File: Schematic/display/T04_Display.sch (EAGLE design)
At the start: 42 parts, among them IC1 4514D, Q1 2N7002, Q2 2N7002, Q3 2N7002, Q4 2N7002, Q5 2N7002, Q6 2N7002, Q7 2N7002, Q8 2N7002, Q9 2N7002

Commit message: V1.1 Schematic, with latches
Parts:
- removed IC1: 4514D, 45xx:4514D
- removed Q1, Q2, Q3, Q4, Q5, Q6, Q7, Q8, Q9: 2N7002, transistor-power:BUZ11BV
- removed R10, R12, R14, R16, R18: 150, resistor:R-US_M3516
- removed R11, R13, R15, R17: 4.7k, resistor:R-US_M3516
- added C10, C11, C12, C13, C14, C5, C6, C7, C8, C9: (no value), resistor:C-EUC1206
- added U$1, U$10, U$12, U$13, U$4, U$5, U$6, U$8, U$9: 2N7002, display:2N7002
- added U$11, U$2, U$7: CD4043, display:CD4043
- added U$3: HEF4067B, display:HEF4067B
- C1, C2, C3, C4: value 0.1u -> (none); device eagle-ltspice:CC3216 -> resistor:C-EUC1206
- LED1, LED4, LED7: value LTL1CHKGKNN -> (none); device led:LEDSMT1206 -> display:LED3MM
- LED2, LED5, LED8: value LTL1CHKSKNN -> (none); device led:LEDSMT1206 -> display:LED3MM
- LED3, LED6, LED9: value LTL1CHKEKNN -> (none); device led:LEDSMT1206 -> display:LED3MM
- R1, R3, R5, R7, R9: value 4.7k -> (none); device resistor:R-US_M3516 -> rcl:R-US_R1206
- R2, R4, R6, R8: value 150 -> (none); device resistor:R-US_M3516 -> rcl:R-US_R1206
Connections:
- removed net +5V: C1.1, C2.1, C3.1, C4.1, IC1A.ST, IC1P.VDD, Q1.D, Q2.D, Q3.D, Q4.D, Q5.D, Q6.D, Q7.D, Q8.D, Q9.D, SV1.2
- removed net BIT0: IC1A.D1, SV1.6
- removed net BIT1: IC1A.D2, SV1.5
- removed net BIT2: IC1A.D3, SV1.4
- removed net BIT3: IC1A.D4, SV1.3
- removed net N$20: LED6.A, R12.1
- removed net N$21: Q7.S, R14.2
- removed net N$24: Q8.S, R16.2
- removed net N$26: Q9.S, R18.2
- removed net N$27: LED9.A, R18.1
- removed net N$28: LED8.A, R16.1
- removed net N$29: LED7.A, R14.1
- removed net N$36: IC1A.S0, Q1.G, R1.2
- removed net N$37: IC1A.S1, Q2.G, R3.2
- removed net N$38: IC1A.S2, Q3.G, R5.2
- removed net N$39: IC1A.S3, Q4.G, R7.2
- removed net N$40: IC1A.S4, Q5.G, R9.2
- removed net N$41: IC1A.S5, Q6.G, R11.2
- removed net N$42: IC1A.S6, Q7.G, R13.2
- removed net N$43: IC1A.S7, Q8.G, R15.2
- removed net N$44: IC1A.S8, Q9.G, R17.2
- new net A0: SV1.6, U$3.A0
- new net A1: SV1.5, U$3.A1
- new net A2: SV1.4, U$3.A2
- new net A3: SV1.3, U$3.A3
- new net BG: U$10.G, U$11.Q1
- new net BR: U$11.Q3, U$13.G
- new net BRES: U$11.R1, U$11.R2, U$11.R3, U$11.R4, U$3.Y3
- new net BS1: U$11.S1, U$3.Y0
- new net BS2: U$11.S2, U$3.Y1
- new net BS3: U$11.S3, U$3.Y2
- new net BY: U$11.Q2, U$12.G
- new net LG: U$1.G, U$2.Q1
- new net LR: U$2.Q3, U$5.G
- new net LRES: U$2.R1, U$2.R2, U$2.R3, U$2.R4, U$3.Y7
- new net LS1: U$2.S1, U$3.Y4
- new net LS2: U$2.S2, U$3.Y5
- new net LS3: U$2.S3, U$3.Y6
- new net LY: U$2.Q2, U$4.G
- new net N$10: LED2.A, R5.1
- new net N$11: R7.2, U$9.S
- new net N$18: LED9.A, R3.1
- new net N$4: R4.2, U$1.S
- new net N$5: LED1.A, R4.1
- new net N$7: R9.2, U$6.S
- new net N$9: LED5.A, R8.1
- new net RG: U$6.G, U$7.Q1
- new net RR: U$7.Q3, U$9.G
- new net RRES: U$3.Y11, U$7.R1, U$7.R2, U$7.R3, U$7.R4
- new net RS1: U$3.Y8, U$7.S1
- new net RS2: U$3.Y9, U$7.S2
- new net RS3: U$3.Y10, U$7.S3
- new net RY: U$7.Q2, U$8.G
- new net VDD: C1.1, C10.1, C11.1, C12.1, C13.2, C14.2, C2.1, C3.1, C4.1, C5.1, C6.1, C7.1, C8.1, C9.1, SV1.1, U$1.D, U$10.D, U$11.EN, U$11.VDD, U$12.D, U$13.D, U$2.EN, U$2.VDD, U$3.VDD, U$3.Z, U$4.D, U$5.D, U$6.D, U$7.EN, U$7.VDD, U$8.D, U$9.D
- net GND: now also C10.2, C11.2, C12.2, C13.1, C14.1, C5.2, C6.2, C7.2, C8.2, C9.2, SV1.2, U$11.S4, U$11.VSS, U$2.S4, U$2.VSS, U$3.E, U$3.VSS, U$7.S4, U$7.VSS; no longer IC1A.INH, IC1P.VSS, R1.1, R11.1, R13.1, R15.1, R17.1, R3.1, R5.1, R7.1, R9.1, SV1.1
- net N$1: now also R5.2, U$4.S; no longer Q1.S, R2.2
- net N$12: now also LED6.A, R7.1; no longer LED2.A, R4.1
- net N$13: now also R1.2, U$10.S; no longer Q4.S, R8.2
- net N$14: now also LED7.A, R1.1; no longer Q5.S, R10.2
- net N$15: now also R2.2, U$12.S; no longer Q6.S, R12.2
- net N$16: now also LED8.A, R2.1; no longer LED5.A, R10.1
- net N$17: now also R3.2, U$13.S; no longer LED4.A, R8.1
- net N$2: now also R8.2, U$8.S; no longer Q2.S, R4.2
- net N$3: now also U$5.S; no longer Q3.S
- net N$8: now also LED4.A, R9.1; no longer LED1.A, R2.1
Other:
- note added: "1.1"
- note removed: "1.0"
- moved on the sheet: C1, C2, C3, C4, LED1, LED2, LED3, LED4, LED5, LED6, LED7, LED8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

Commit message: Preliminary Board Layout Rev.1
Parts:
- renumbered U$11 to LEFT, U$2 to REAR, U$7 to RIGHT

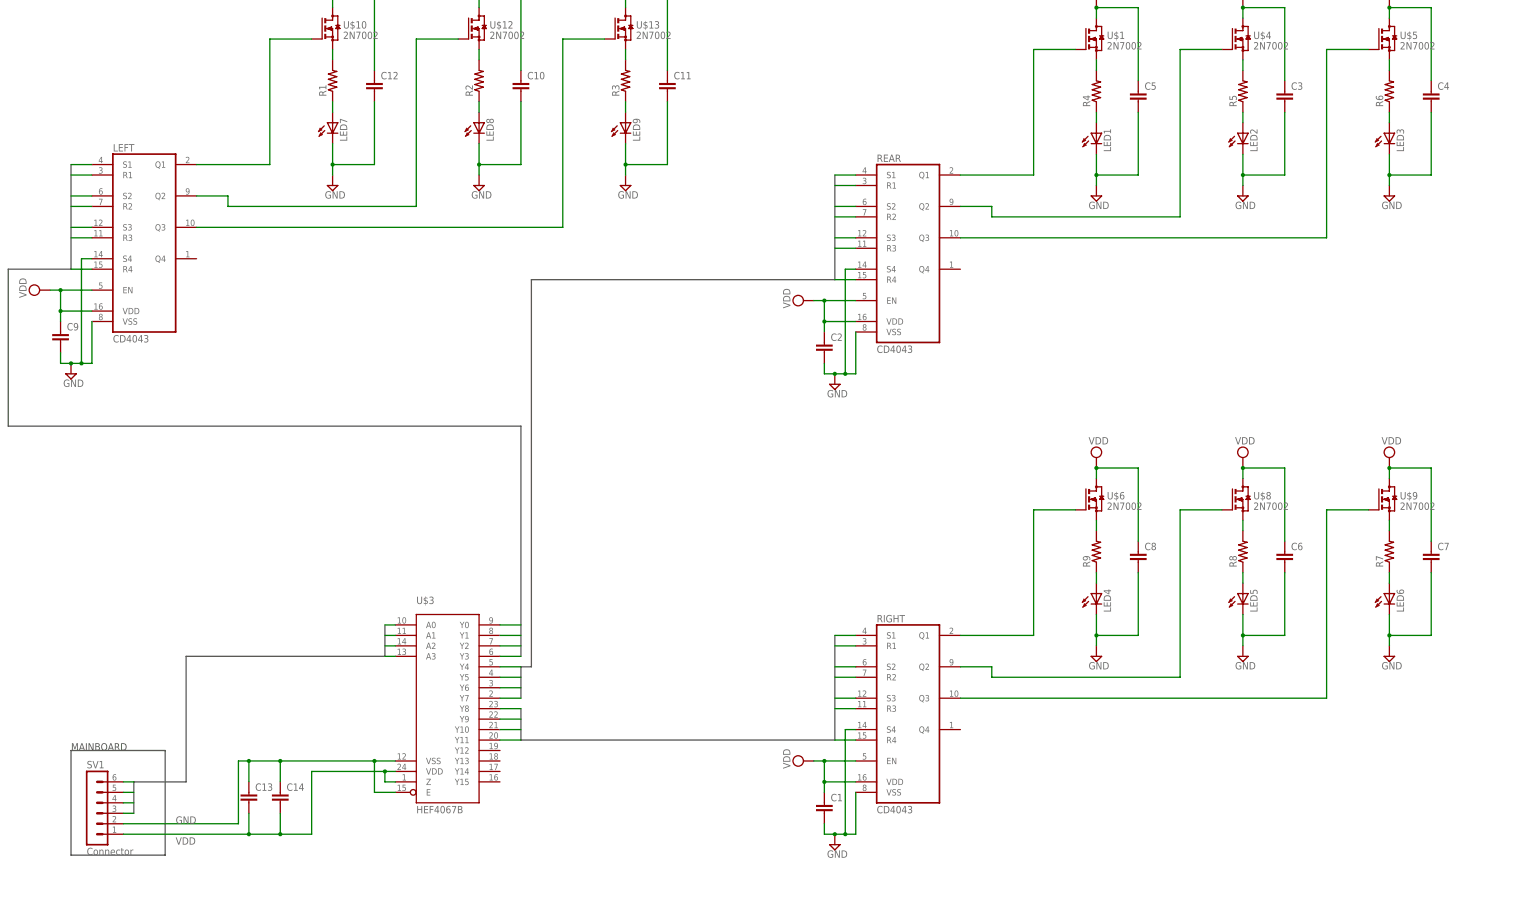
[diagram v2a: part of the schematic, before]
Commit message: Reverified ERC/DRC for assignment files, added version summery.
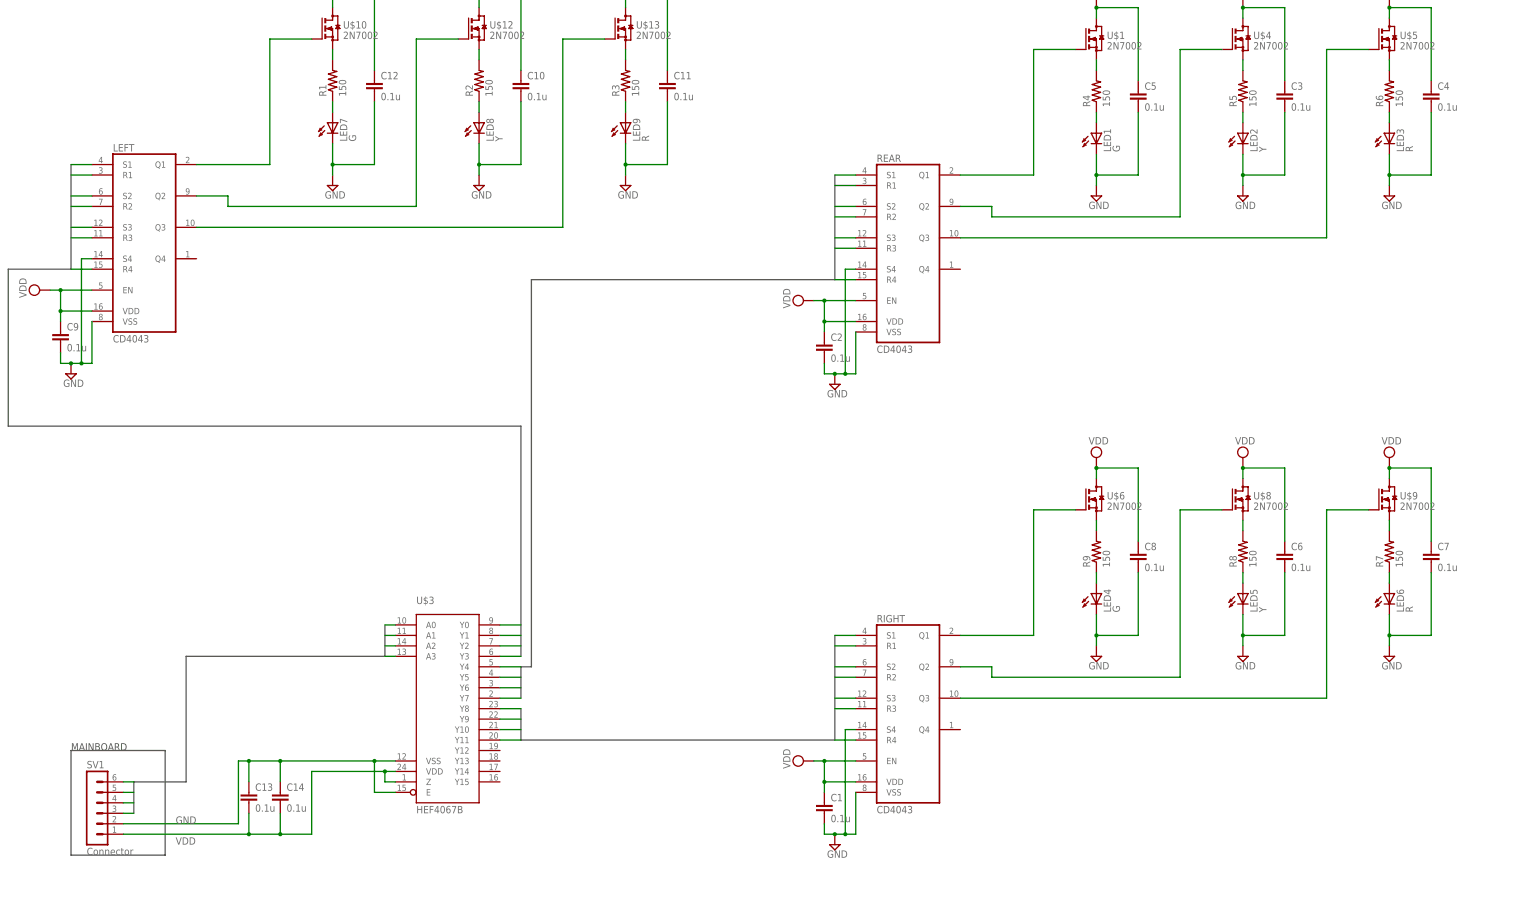
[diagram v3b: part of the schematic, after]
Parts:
- C1, C10, C11, C12, C13, C14, C2, C3, C4, C5, C6, C7, C8, C9: value (none) -> 0.1u
- LED1, LED4, LED7: value (none) -> G
- LED2, LED5, LED8: value (none) -> Y
- LED3, LED6, LED9: value (none) -> R
- R1, R2, R3, R4, R5, R6, R7, R8, R9: value (none) -> 150
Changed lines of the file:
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@@
 <?xml version="1.0" encoding="utf-8"?>
 <!DOCTYPE eagle SYSTEM "eagle.dtd">
-<eagle version="7.1.0">
+<eagle version="6.3">
 <drawing>
 <settings>
@@
 <part name="REAR" library="display" deviceset="CD4043" device=""/>
 <part name="U$3" library="display" deviceset="HEF4067B" device=""/>
-<part name="LED1" library="display" deviceset="LED" device="3MM"/>
+<part name="LED1" library="display" deviceset="LED" device="3MM" value="G"/>
 <part name="SUPPLY1" library="supply2" deviceset="GND" device=""/>
 <part name="SUPPLY2" library="supply2" deviceset="VDD" device=""/>
 <part name="U$4" library="display" deviceset="2N7002" device=""/>
-<part name="LED2" library="display" deviceset="LED" device="3MM"/>
+<part name="LED2" library="display" deviceset="LED" device="3MM" value="Y"/>
 <part name="SUPPLY3" library="supply2" deviceset="GND" device=""/>
 <part name="SUPPLY4" library="supply2" deviceset="VDD" device=""/>
 <part name="U$5" library="display" deviceset="2N7002" device=""/>
-<part name="LED3" library="display" deviceset="LED" device="3MM"/>
+<part name="LED3" library="display" deviceset="LED" device="3MM" value="R"/>
 <part name="SUPPLY5" library="supply2" deviceset="GND" device=""/>
 <part name="SUPPLY6" library="supply2" deviceset="VDD" device=""/>
 <part name="SUPPLY7" library="supply2" deviceset="VDD" device=""/>
-<part name="C2" library="resistor" deviceset="C-EU" device="C1206"/>
+<part name="C2" library="resistor" deviceset="C-EU" device="C1206" value="0.1u"/>
 <part name="SUPPLY8" library="supply2" deviceset="GND" device=""/>
-<part name="C3" library="resistor" deviceset="C-EU" device="C1206"/>
-<part name="C4" library="resistor" deviceset="C-EU" device="C1206"/>
-<part name="C5" library="resistor" deviceset="C-EU" device="C1206"/>
+<part name="C3" library="resistor" deviceset="C-EU" device="C1206" value="0.1u"/>
+<part name="C4" library="resistor" deviceset="C-EU" device="C1206" value="0.1u"/>
+<part name="C5" library="resistor" deviceset="C-EU" device="C1206" value="0.1u"/>
 <part name="U$6" library="display" deviceset="2N7002" device=""/>
 <part name="RIGHT" library="display" deviceset="CD4043" device=""/>
-<part name="LED4" library="display" deviceset="LED" device="3MM"/>
+<part name="LED4" library="display" deviceset="LED" device="3MM" value="G"/>
 <part name="SUPPLY9" library="supply2" deviceset="GND" device=""/>
 <part name="SUPPLY10" library="supply2" deviceset="VDD" device=""/>
 <part name="U$8" library="display" deviceset="2N7002" device=""/>
-<part name="LED5" library="display" deviceset="LED" device="3MM"/>
+<part name="LED5" library="display" deviceset="LED" device="3MM" value="Y"/>
 <part name="SUPPLY11" library="supply2" deviceset="GND" device=""/>
 <part name="SUPPLY12" library="supply2" deviceset="VDD" device=""/>
 <part name="U$9" library="display" deviceset="2N7002" device=""/>
-<part name="LED6" library="display" deviceset="LED" device="3MM"/>
+<part name="LED6" library="display" deviceset="LED" device="3MM" value="R"/>
 <part name="SUPPLY13" library="supply2" deviceset="GND" device=""/>
 <part name="SUPPLY14" library="supply2" deviceset="VDD" device=""/>
 <part name="SUPPLY15" library="supply2" deviceset="VDD" device=""/>
-<part name="C1" library="resistor" deviceset="C-EU" device="C1206"/>
+<part name="C1" library="resistor" deviceset="C-EU" device="C1206" value="0.1u"/>
 <part name="SUPPLY16" library="supply2" deviceset="GND" device=""/>
-<part name="C6" library="resistor" deviceset="C-EU" device="C1206"/>
-<part name="C7" library="resistor" deviceset="C-EU" device="C1206"/>
-<part name="C8" library="resistor" deviceset="C-EU" device="C1206"/>
+<part name="C6" library="resistor" deviceset="C-EU" device="C1206" value="0.1u"/>
+<part name="C7" library="resistor" deviceset="C-EU" device="C1206" value="0.1u"/>
+<part name="C8" library="resistor" deviceset="C-EU" device="C1206" value="0.1u"/>
 <part name="U$10" library="display" deviceset="2N7002" device=""/>
 <part name="LEFT" library="display" deviceset="CD4043" device=""/>
-<part name="LED7" library="display" deviceset="LED" device="3MM"/>
+<part name="LED7" library="display" deviceset="LED" device="3MM" value="G"/>
 <part name="SUPPLY17" library="supply2" deviceset="GND" device=""/>
 <part name="SUPPLY18" library="supply2" deviceset="VDD" device=""/>
 <part name="U$12" library="display" deviceset="2N7002" device=""/>
-<part name="LED8" library="display" deviceset="LED" device="3MM"/>
+<part name="LED8" library="display" deviceset="LED" device="3MM" value="Y"/>
 <part name="SUPPLY19" library="supply2" deviceset="GND" device=""/>
 <part name="SUPPLY20" library="supply2" deviceset="VDD" device=""/>
 <part name="U$13" library="display" deviceset="2N7002" device=""/>
-<part name="LED9" library="display" deviceset="LED" device="3MM"/>
+<part name="LED9" library="display" deviceset="LED" device="3MM" value="R"/>
 <part name="SUPPLY21" library="supply2" deviceset="GND" device=""/>
 <part name="SUPPLY22" library="supply2" deviceset="VDD" device=""/>
 <part name="SUPPLY23" library="supply2" deviceset="VDD" device=""/>
-<part name="C9" library="resistor" deviceset="C-EU" device="C1206"/>
+<part name="C9" library="resistor" deviceset="C-EU" device="C1206" value="0.1u"/>
 <part name="SUPPLY24" library="supply2" deviceset="GND" device=""/>
-<part name="C10" library="resistor" deviceset="C-EU" device="C1206"/>
-<part name="C11" library="resistor" deviceset="C-EU" device="C1206"/>
-<part name="C12" library="resistor" deviceset="C-EU" device="C1206"/>
-<part name="C13" library="resistor" deviceset="C-EU" device="C1206"/>
-<part name="C14" library="resistor" deviceset="C-EU" device="C1206"/>
-<part name="R1" library="rcl" deviceset="R-US_" device="R1206"/>
-<part name="R2" library="rcl" deviceset="R-US_" device="R1206"/>
-<part name="R3" library="rcl" deviceset="R-US_" device="R1206"/>
-<part name="R4" library="rcl" deviceset="R-US_" device="R1206"/>
-<part name="R5" library="rcl" deviceset="R-US_" device="R1206"/>
-<part name="R6" library="rcl" deviceset="R-US_" device="R1206"/>
-<part name="R7" library="rcl" deviceset="R-US_" device="R1206"/>
-<part name="R8" library="rcl" deviceset="R-US_" device="R1206"/>
-<part name="R9" library="rcl" deviceset="R-US_" device="R1206"/>
+<part name="C10" library="resistor" deviceset="C-EU" device="C1206" value="0.1u"/>
+<part name="C11" library="resistor" deviceset="C-EU" device="C1206" value="0.1u"/>
+<part name="C12" library="resistor" deviceset="C-EU" device="C1206" value="0.1u"/>
+<part name="C13" library="resistor" deviceset="C-EU" device="C1206" value="0.1u"/>
+<part name="C14" library="resistor" deviceset="C-EU" device="C1206" value="0.1u"/>
+<part name="R1" library="rcl" deviceset="R-US_" device="R1206" value="150"/>
+<part name="R2" library="rcl" deviceset="R-US_" device="R1206" value="150"/>
+<part name="R3" library="rcl" deviceset="R-US_" device="R1206" value="150"/>
+<part name="R4" library="rcl" deviceset="R-US_" device="R1206" value="150"/>
+<part name="R5" library="rcl" deviceset="R-US_" device="R1206" value="150"/>
+<part name="R6" library="rcl" deviceset="R-US_" device="R1206" value="150"/>
+<part name="R7" library="rcl" deviceset="R-US_" device="R1206" value="150"/>
+<part name="R8" library="rcl" deviceset="R-US_" device="R1206" value="150"/>
+<part name="R9" library="rcl" deviceset="R-US_" device="R1206" value="150"/>
 </parts>
 <sheets>
@@
 </sheet>
 </sheets>
+<errors>
+</errors>
 </schematic>
 </drawing>
